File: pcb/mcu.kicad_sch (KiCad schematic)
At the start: 18 parts, among them J9 DNP, SW1 SKRKAEE020, SW2 SKRKAEE020, U7 ESP32-S3-WROOM-1

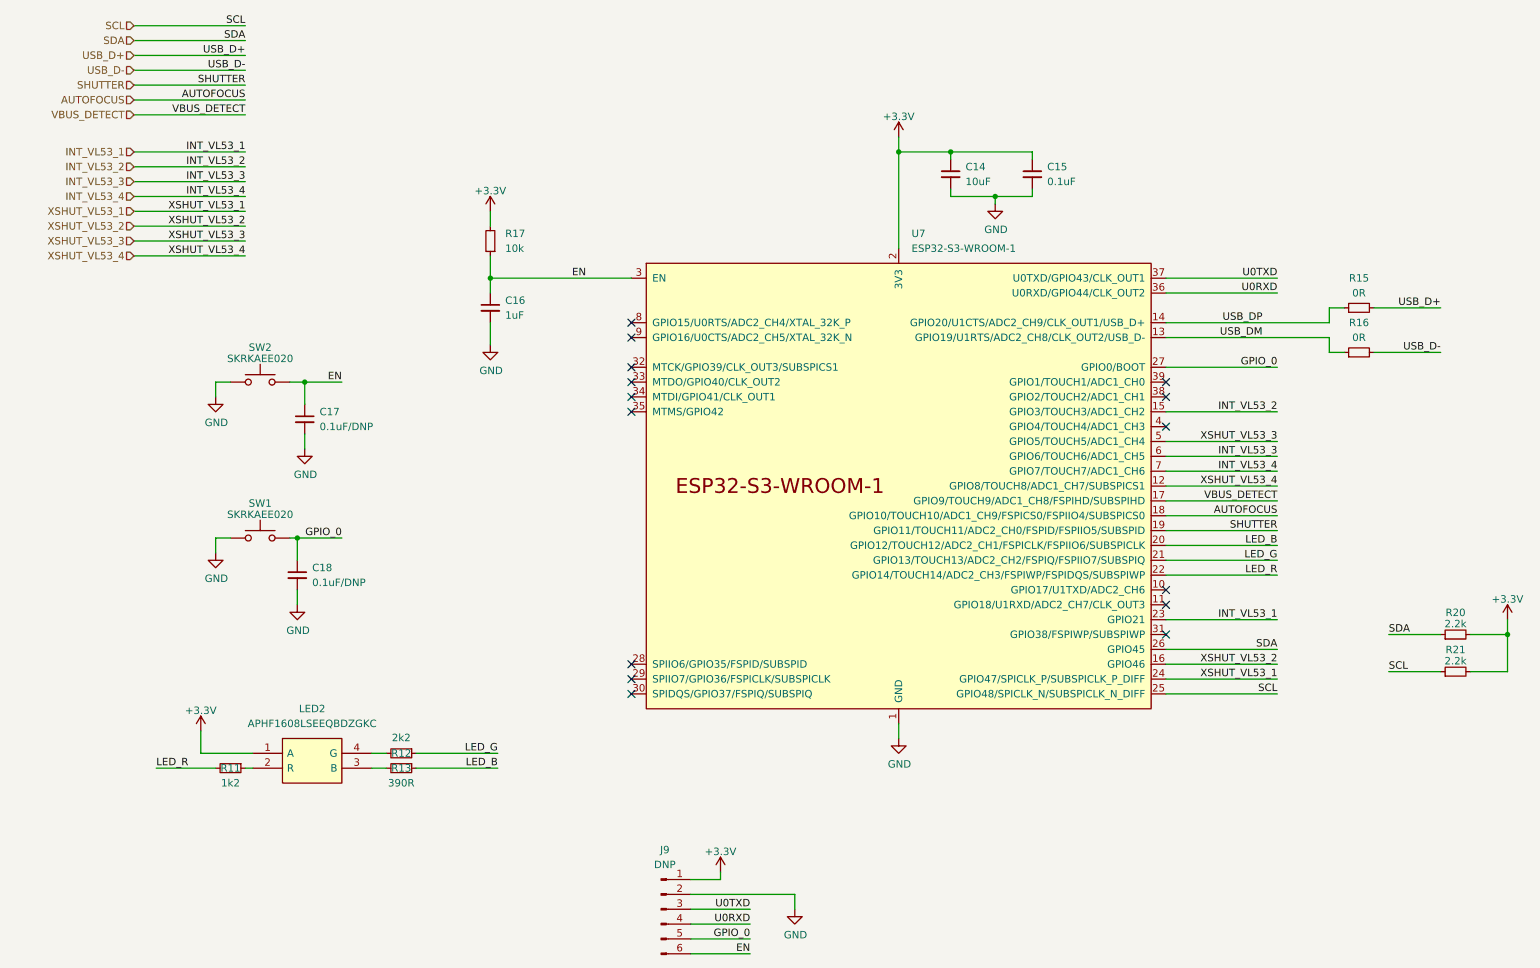
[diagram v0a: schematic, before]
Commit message: Changed net names to match functionallity of active low
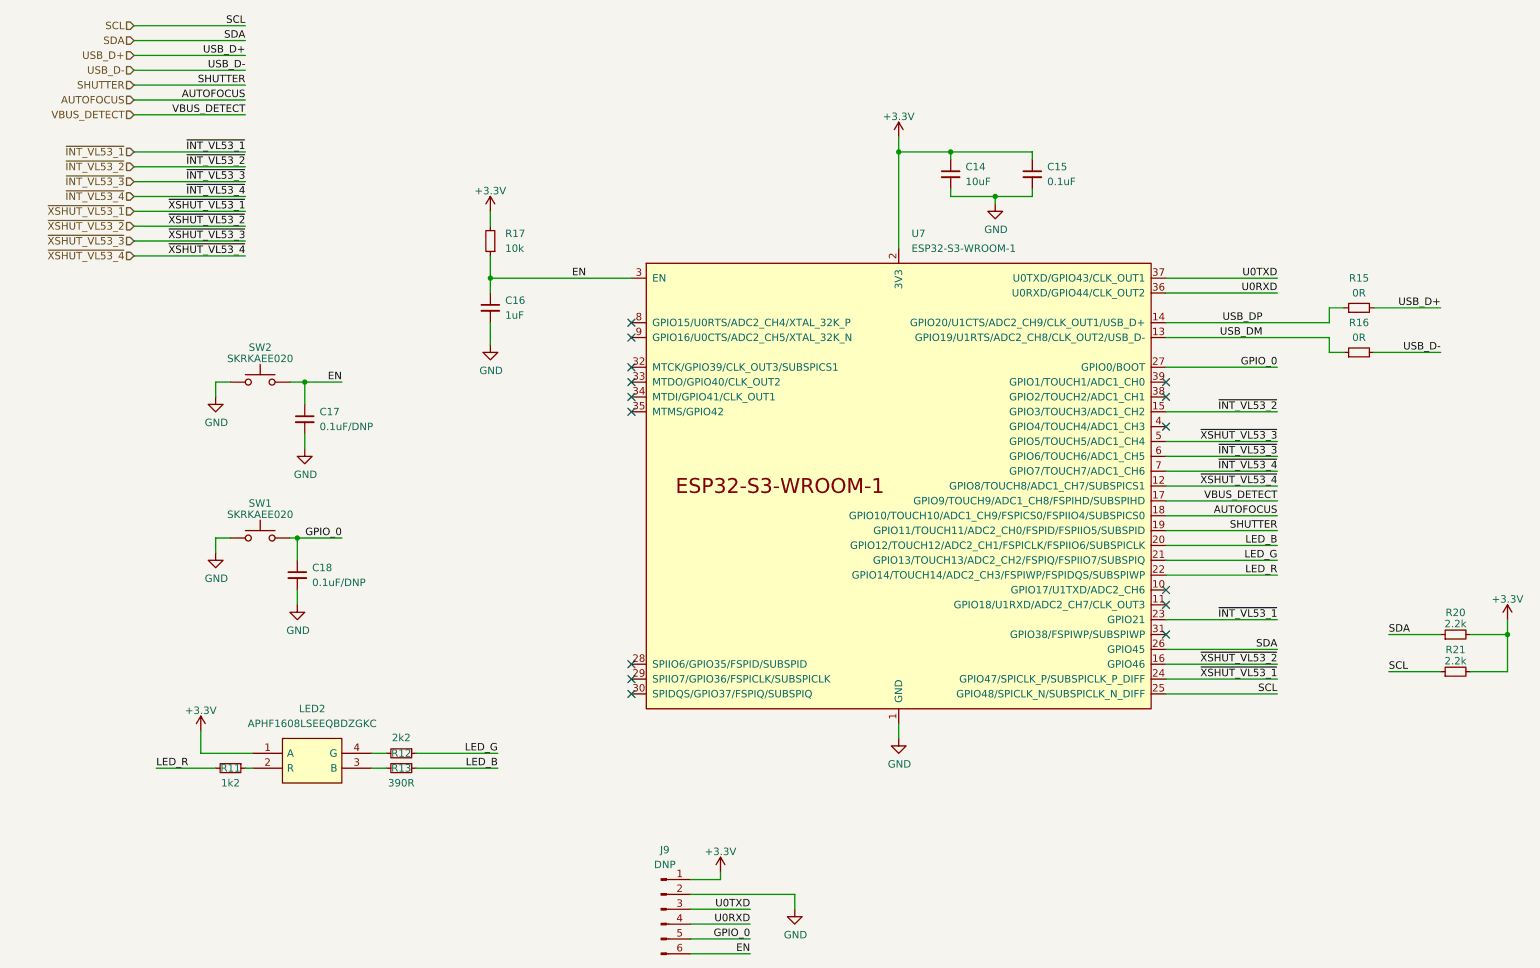
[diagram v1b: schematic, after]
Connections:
- net INT_VL53_1 renamed ~{INT_VL53_1}
- net INT_VL53_2 renamed ~{INT_VL53_2}
- net INT_VL53_3 renamed ~{INT_VL53_3}
- net INT_VL53_4 renamed ~{INT_VL53_4}
- net XSHUT_VL53_1 renamed ~{XSHUT_VL53_1}
- net XSHUT_VL53_2 renamed ~{XSHUT_VL53_2}
- net XSHUT_VL53_3 renamed ~{XSHUT_VL53_3}
- net XSHUT_VL53_4 renamed ~{XSHUT_VL53_4}
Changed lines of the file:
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@@
     (effects (font (size 1.27 1.27)) (justify right bottom))
   )
-  (label "INT_VL53_2" (at 48.26 40.64 180) (fields_autoplaced)
+  (label "~{INT_VL53_2}" (at 48.26 40.64 180) (fields_autoplaced)
     (effects (font (size 1.27 1.27)) (justify right bottom))
   )
@@
     (effects (font (size 1.27 1.27)) (justify right bottom))
   )
-  (label "INT_VL53_4" (at 48.26 45.72 180) (fields_autoplaced)
+  (label "~{INT_VL53_4}" (at 48.26 45.72 180) (fields_autoplaced)
     (effects (font (size 1.27 1.27)) (justify right bottom))
   )
@@
     (effects (font (size 1.27 1.27)) (justify right bottom))
   )
-  (label "XSHUT_VL53_1" (at 224.79 128.27 180) (fields_autoplaced)
+  (label "~{XSHUT_VL53_1}" (at 224.79 128.27 180) (fields_autoplaced)
     (effects (font (size 1.27 1.27)) (justify right bottom))
   )
-  (label "INT_VL53_4" (at 224.79 92.71 180) (fields_autoplaced)
+  (label "~{INT_VL53_4}" (at 224.79 92.71 180) (fields_autoplaced)
     (effects (font (size 1.27 1.27)) (justify right bottom))
   )
-  (label "INT_VL53_3" (at 48.26 43.18 180) (fields_autoplaced)
+  (label "~{INT_VL53_3}" (at 48.26 43.18 180) (fields_autoplaced)
     (effects (font (size 1.27 1.27)) (justify right bottom))
   )
@@
     (effects (font (size 1.27 1.27)) (justify right bottom))
   )
-  (label "INT_VL53_2" (at 224.79 82.55 180) (fields_autoplaced)
+  (label "~{INT_VL53_2}" (at 224.79 82.55 180) (fields_autoplaced)
     (effects (font (size 1.27 1.27)) (justify right bottom))
   )
@@
     (effects (font (size 1.27 1.27)) (justify left bottom))
   )
-  (label "XSHUT_VL53_2" (at 224.79 125.73 180) (fields_autoplaced)
+  (label "~{XSHUT_VL53_2}" (at 224.79 125.73 180) (fields_autoplaced)
     (effects (font (size 1.27 1.27)) (justify right bottom))
   )
-  (label "INT_VL53_3" (at 224.79 90.17 180) (fields_autoplaced)
+  (label "~{INT_VL53_3}" (at 224.79 90.17 180) (fields_autoplaced)
     (effects (font (size 1.27 1.27)) (justify right bottom))
   )
-  (label "INT_VL53_1" (at 224.79 118.11 180) (fields_autoplaced)
+  (label "~{INT_VL53_1}" (at 224.79 118.11 180) (fields_autoplaced)
     (effects (font (size 1.27 1.27)) (justify right bottom))
   )
-  (label "INT_VL53_1" (at 48.26 38.1 180) (fields_autoplaced)
+  (label "~{INT_VL53_1}" (at 48.26 38.1 180) (fields_autoplaced)
     (effects (font (size 1.27 1.27)) (justify right bottom))
   )
@@
     (effects (font (size 1.27 1.27)) (justify left bottom))
   )
-  (label "XSHUT_VL53_2" (at 48.26 50.8 180) (fields_autoplaced)
+  (label "~{XSHUT_VL53_2}" (at 48.26 50.8 180) (fields_autoplaced)
     (effects (font (size 1.27 1.27)) (justify right bottom))
   )
@@
     (effects (font (size 1.27 1.27)) (justify right bottom))
   )
-  (label "XSHUT_VL53_3" (at 48.26 53.34 180) (fields_autoplaced)
+  (label "~{XSHUT_VL53_3}" (at 48.26 53.34 180) (fields_autoplaced)
     (effects (font (size 1.27 1.27)) (justify right bottom))
   )
@@
     (effects (font (size 1.27 1.27)) (justify right bottom))
   )
-  (label "XSHUT_VL53_4" (at 224.79 95.25 180) (fields_autoplaced)
+  (label "~{XSHUT_VL53_4}" (at 224.79 95.25 180) (fields_autoplaced)
     (effects (font (size 1.27 1.27)) (justify right bottom))
   )
@@
     (effects (font (size 1.27 1.27)) (justify right bottom))
   )
-  (label "XSHUT_VL53_3" (at 224.79 87.63 180) (fields_autoplaced)
+  (label "~{XSHUT_VL53_3}" (at 224.79 87.63 180) (fields_autoplaced)
     (effects (font (size 1.27 1.27)) (justify right bottom))
   )
-  (label "XSHUT_VL53_1" (at 48.26 48.26 180) (fields_autoplaced)
+  (label "~{XSHUT_VL53_1}" (at 48.26 48.26 180) (fields_autoplaced)
     (effects (font (size 1.27 1.27)) (justify right bottom))
   )
-  (label "XSHUT_VL53_4" (at 48.26 55.88 180) (fields_autoplaced)
+  (label "~{XSHUT_VL53_4}" (at 48.26 55.88 180) (fields_autoplaced)
     (effects (font (size 1.27 1.27)) (justify right bottom))
   )
@@
     (effects (font (size 1.27 1.27)) (justify right bottom))
   )
-  (hierarchical_label "INT_VL53_3" (shape input) (at 29.21 43.18 180) (fields_autoplaced)
+  (hierarchical_label "~{INT_VL53_3}" (shape input) (at 29.21 43.18 180) (fields_autoplaced)
     (effects (font (size 1.27 1.27)) (justify right))
   )
@@
     (effects (font (size 1.27 1.27)) (justify right))
   )
-  (hierarchical_label "XSHUT_VL53_4" (shape input) (at 29.21 55.88 180) (fields_autoplaced)
+  (hierarchical_label "~{XSHUT_VL53_4}" (shape input) (at 29.21 55.88 180) (fields_autoplaced)
     (effects (font (size 1.27 1.27)) (justify right))
   )
@@
     (effects (font (size 1.27 1.27)) (justify right))
   )
-  (hierarchical_label "XSHUT_VL53_2" (shape input) (at 29.21 50.8 180) (fields_autoplaced)
+  (hierarchical_label "~{XSHUT_VL53_2}" (shape input) (at 29.21 50.8 180) (fields_autoplaced)
     (effects (font (size 1.27 1.27)) (justify right))
   )
@@
     (effects (font (size 1.27 1.27)) (justify right))
   )
-  (hierarchical_label "XSHUT_VL53_1" (shape input) (at 29.21 48.26 180) (fields_autoplaced)
+  (hierarchical_label "~{XSHUT_VL53_1}" (shape input) (at 29.21 48.26 180) (fields_autoplaced)
     (effects (font (size 1.27 1.27)) (justify right))
   )
@@
     (effects (font (size 1.27 1.27)) (justify right))
   )
-  (hierarchical_label "INT_VL53_1" (shape input) (at 29.21 38.1 180) (fields_autoplaced)
+  (hierarchical_label "~{INT_VL53_1}" (shape input) (at 29.21 38.1 180) (fields_autoplaced)
     (effects (font (size 1.27 1.27)) (justify right))
   )
@@
     (effects (font (size 1.27 1.27)) (justify right))
   )
-  (hierarchical_label "INT_VL53_2" (shape input) (at 29.21 40.64 180) (fields_autoplaced)
+  (hierarchical_label "~{INT_VL53_2}" (shape input) (at 29.21 40.64 180) (fields_autoplaced)
     (effects (font (size 1.27 1.27)) (justify right))
   )
-  (hierarchical_label "XSHUT_VL53_3" (shape input) (at 29.21 53.34 180) (fields_autoplaced)
+  (hierarchical_label "~{XSHUT_VL53_3}" (shape input) (at 29.21 53.34 180) (fields_autoplaced)
     (effects (font (size 1.27 1.27)) (justify right))
   )
@@
     (effects (font (size 1.27 1.27)) (justify right))
   )
-  (hierarchical_label "INT_VL53_4" (shape input) (at 29.21 45.72 180) (fields_autoplaced)
+  (hierarchical_label "~{INT_VL53_4}" (shape input) (at 29.21 45.72 180) (fields_autoplaced)
     (effects (font (size 1.27 1.27)) (justify right))
   )

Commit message: Moved magnet switch to the other side
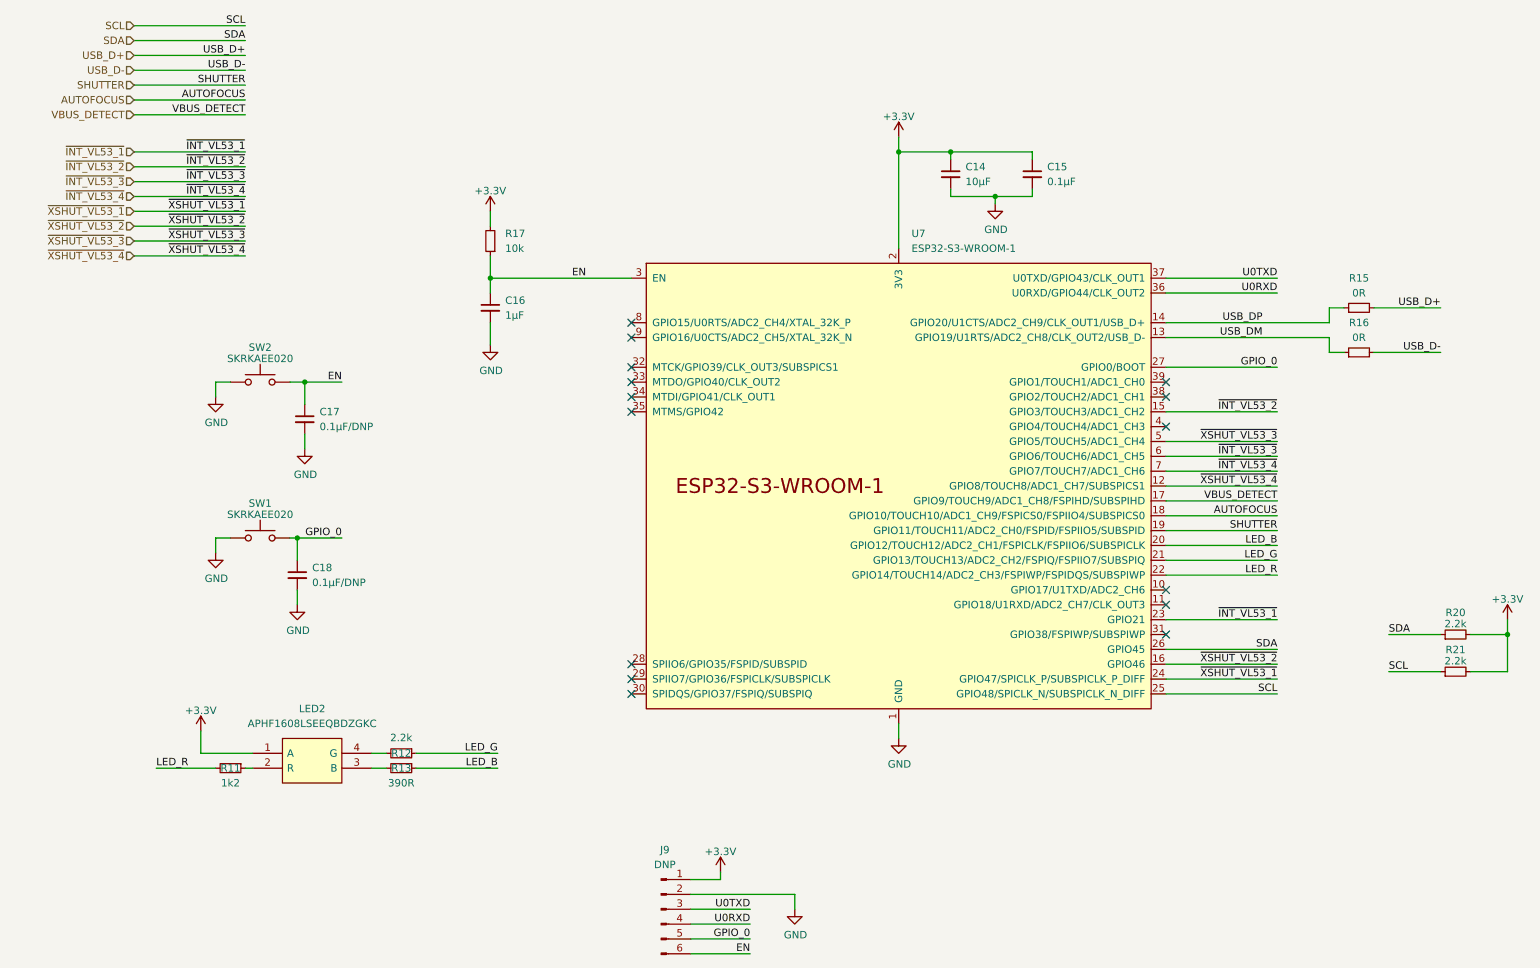
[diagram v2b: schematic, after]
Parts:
- C14: value 10uF -> 10µF
- C15: value 0.1uF -> 0.1µF
- C16: value 1uF -> 1µF
- C17, C18: value 0.1uF/DNP -> 0.1µF/DNP
- R12: value 2k2 -> 2.2k
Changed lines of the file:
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@@
       (effects (font (size 1.27 1.27)) (justify left))
     )
-    (property "Value" "0.1uF/DNP" (at 59.69 111.7663 0)
+    (property "Value" "0.1µF/DNP" (at 59.69 111.7663 0)
       (effects (font (size 1.27 1.27)) (justify left))
     )
@@
       (effects (font (size 1.27 1.27)) (justify left))
     )
-    (property "Value" "0.1uF" (at 185.42 43.1863 0)
+    (property "Value" "0.1µF" (at 185.42 43.1863 0)
       (effects (font (size 1.27 1.27)) (justify left))
     )
@@
       (effects (font (size 1.27 1.27)) (justify left))
     )
-    (property "Value" "10uF" (at 171.45 43.1863 0)
+    (property "Value" "10µF" (at 171.45 43.1863 0)
       (effects (font (size 1.27 1.27)) (justify left))
     )
@@
       (effects (font (size 1.27 1.27)) (justify left))
     )
-    (property "Value" "0.1uF/DNP" (at 60.96 85.0963 0)
+    (property "Value" "0.1µF/DNP" (at 60.96 85.0963 0)
       (effects (font (size 1.27 1.27)) (justify left))
     )
@@
       (effects (font (size 1.27 1.27)))
     )
-    (property "Value" "2k2" (at 74.93 138.303 90)
+    (property "Value" "2.2k" (at 74.93 138.303 90)
       (effects (font (size 1.27 1.27)))
     )
@@
       (effects (font (size 1.27 1.27)) (justify left))
     )
-    (property "Value" "1uF" (at 92.71 66.0463 0)
-      (effects (font (size 1.27 1.27)) (justify left))
-    )
+    (property "Value" "1µF" (at 92.71 66.0463 0)
+      (effects (font (size 1.27 1.27)) (justify left))
+    )

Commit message: Updated footprints try to fix DRC
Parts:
- J9: now left out of the parts list
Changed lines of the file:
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@@
   )
   (symbol (lib_id "Connector:Conn_01x06_Pin") (at 119.38 167.64 0) (unit 1)
-    (in_bom yes) (on_board yes) (dnp no) (fields_autoplaced)
+    (in_bom no) (on_board yes) (dnp no) (fields_autoplaced)
     (property "Reference" "J9" (at 120.015 157.48 0)
       (effects (font (size 1.27 1.27)))

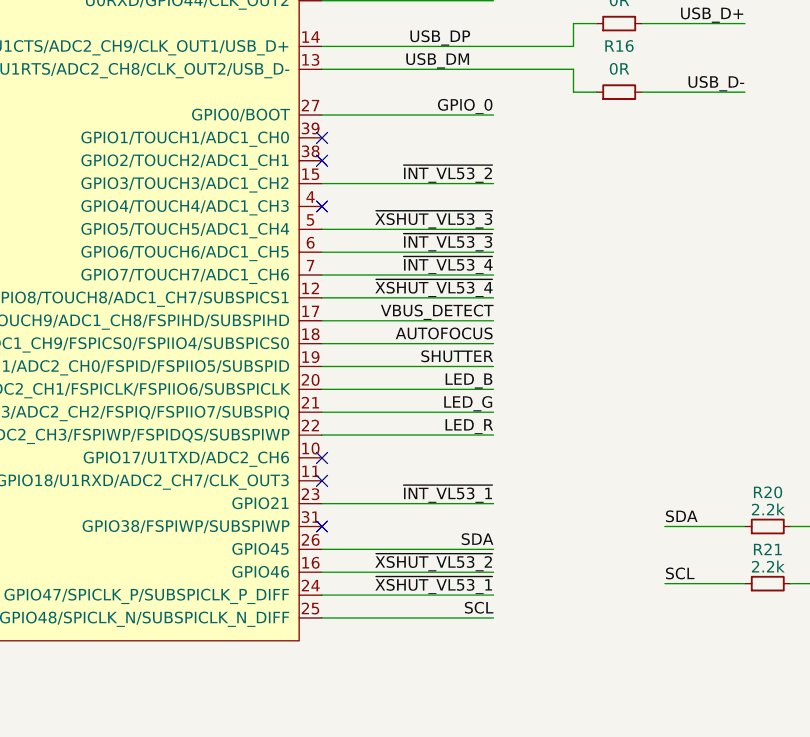
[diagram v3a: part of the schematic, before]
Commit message: Fixed usage of strapping pins
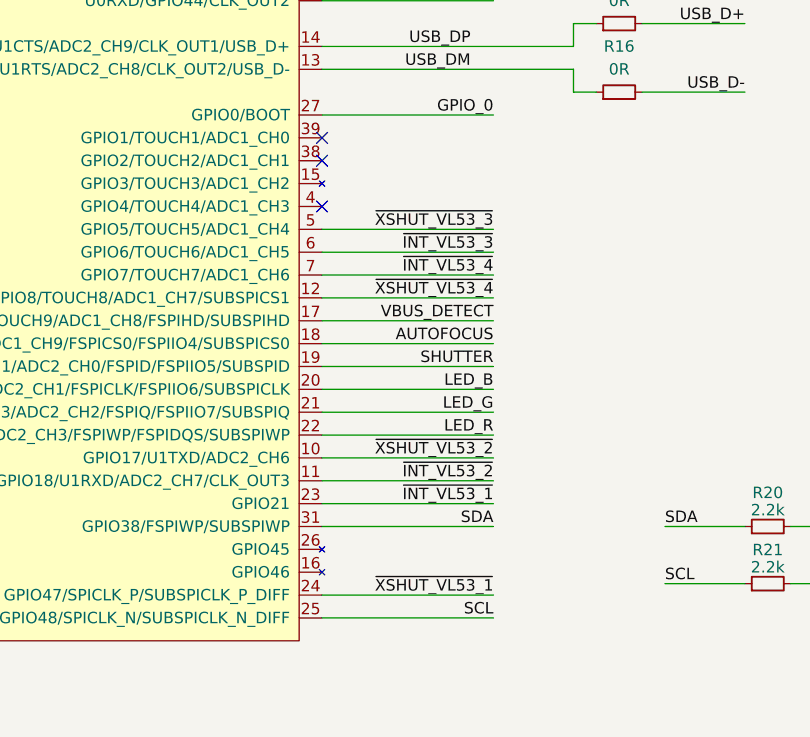
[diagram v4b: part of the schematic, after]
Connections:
- net SDA: now also U7.31 (GPIO38/FSPIWP/SUBSPIWP); no longer U7.26 (GPIO45)
- net ~{INT_VL53_2}: now also U7.11 (GPIO18/U1RXD/ADC2_CH7/CLK_OUT3); no longer U7.15 (GPIO3/TOUCH3/ADC1_CH2)
- net ~{XSHUT_VL53_2}: now also U7.10 (GPIO17/U1TXD/ADC2_CH6); no longer U7.16 (GPIO46)
- no-connect marks 15 -> 12
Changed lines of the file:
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@@
   (no_connect (at 114.3 74.93))
   (no_connect (at 114.3 82.55))
-  (no_connect (at 205.74 115.57))
-  (no_connect (at 205.74 120.65))
   (no_connect (at 114.3 125.73))
   (no_connect (at 205.74 77.47))
   (no_connect (at 114.3 128.27))
-  (no_connect (at 205.74 113.03))
   (no_connect (at 114.3 69.85))
   (no_connect (at 114.3 67.31))
@@
     (stroke (width 0) (type default))
   )
-  (wire (pts (xy 205.74 123.19) (xy 224.79 123.19))
-    (stroke (width 0) (type default))
-  )
-  (wire (pts (xy 205.74 125.73) (xy 224.79 125.73))
+  (wire (pts (xy 205.74 120.65) (xy 224.79 120.65))
     (stroke (width 0) (type default))
   )
@@
     (stroke (width 0) (type default))
   )
+  (wire (pts (xy 205.74 113.03) (xy 224.79 113.03))
+    (stroke (width 0) (type default))
+  )
   (wire (pts (xy 264.16 120.65) (xy 257.81 120.65))
     (stroke (width 0) (type default))
@@
     (stroke (width 0) (type default))
   )
-  (wire (pts (xy 205.74 82.55) (xy 224.79 82.55))
+  (wire (pts (xy 205.74 115.57) (xy 224.79 115.57))
     (stroke (width 0) (type default))
   )
@@
     (effects (font (size 1.27 1.27)) (justify right bottom))
   )
-  (label "~{INT_VL53_2}" (at 224.79 82.55 180) (fields_autoplaced)
+  (label "~{INT_VL53_2}" (at 224.79 115.57 180) (fields_autoplaced)
     (effects (font (size 1.27 1.27)) (justify right bottom))
   )
@@
     (effects (font (size 1.27 1.27)) (justify left bottom))
   )
-  (label "~{XSHUT_VL53_2}" (at 224.79 125.73 180) (fields_autoplaced)
+  (label "~{XSHUT_VL53_2}" (at 224.79 113.03 180) (fields_autoplaced)
     (effects (font (size 1.27 1.27)) (justify right bottom))
   )
@@
     (effects (font (size 1.27 1.27)) (justify right bottom))
   )
-  (label "SDA" (at 224.79 123.19 180) (fields_autoplaced)
+  (label "SDA" (at 224.79 120.65 180) (fields_autoplaced)
     (effects (font (size 1.27 1.27)) (justify right bottom))
   )
@@
     (pin "13")
     (pin "14")
-    (pin "15")
-    (pin "16")
     (pin "17")
     (pin "18")
@@
     (pin "24")
     (pin "25")
-    (pin "26")
     (pin "27")
     (pin "28")
@@
     (pin "8")
     (pin "9")
-    (instances
-      (project "rep-trap-pcb"
+    (pin "15")
+    (pin "16")
+    (pin "26")
+    (instances
+      (project "rep-trap-pcb"
